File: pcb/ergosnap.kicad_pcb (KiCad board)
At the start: 2 copper layers, 133.6 x 132.2 mm, 41 parts, among them J0 Conn_01x05_Female, J1 5PIN, SW1 switch_diode, SW10 switch_diode, SW11 switch_diode, SW12 switch_diode, SW13 switch_diode, SW14 switch_diode, SW15 switch_diode, SW16 switch_diode, SW17 switch_diode, SW18 switch_diode, SW19 switch_diode, SW2 switch_diode, SW20 switch_diode, SW21 switch_diode, SW22 switch_diode, SW23 switch_diode, SW24 switch_diode, SW25 switch_diode, SW26 switch_diode, SW27 switch_diode, SW28 switch_diode, SW3 switch_diode, SW30 switch_diode, SW31 switch_diode, SW32 switch_diode, SW33 switch_diode, SW34 switch_diode, SW35 switch_diode, SW4 switch_diode, SW5 switch_diode, SW6 switch_diode, SW7 switch_diode, SW8 switch_diode, SW9 switch_diode, U3 ProMicro

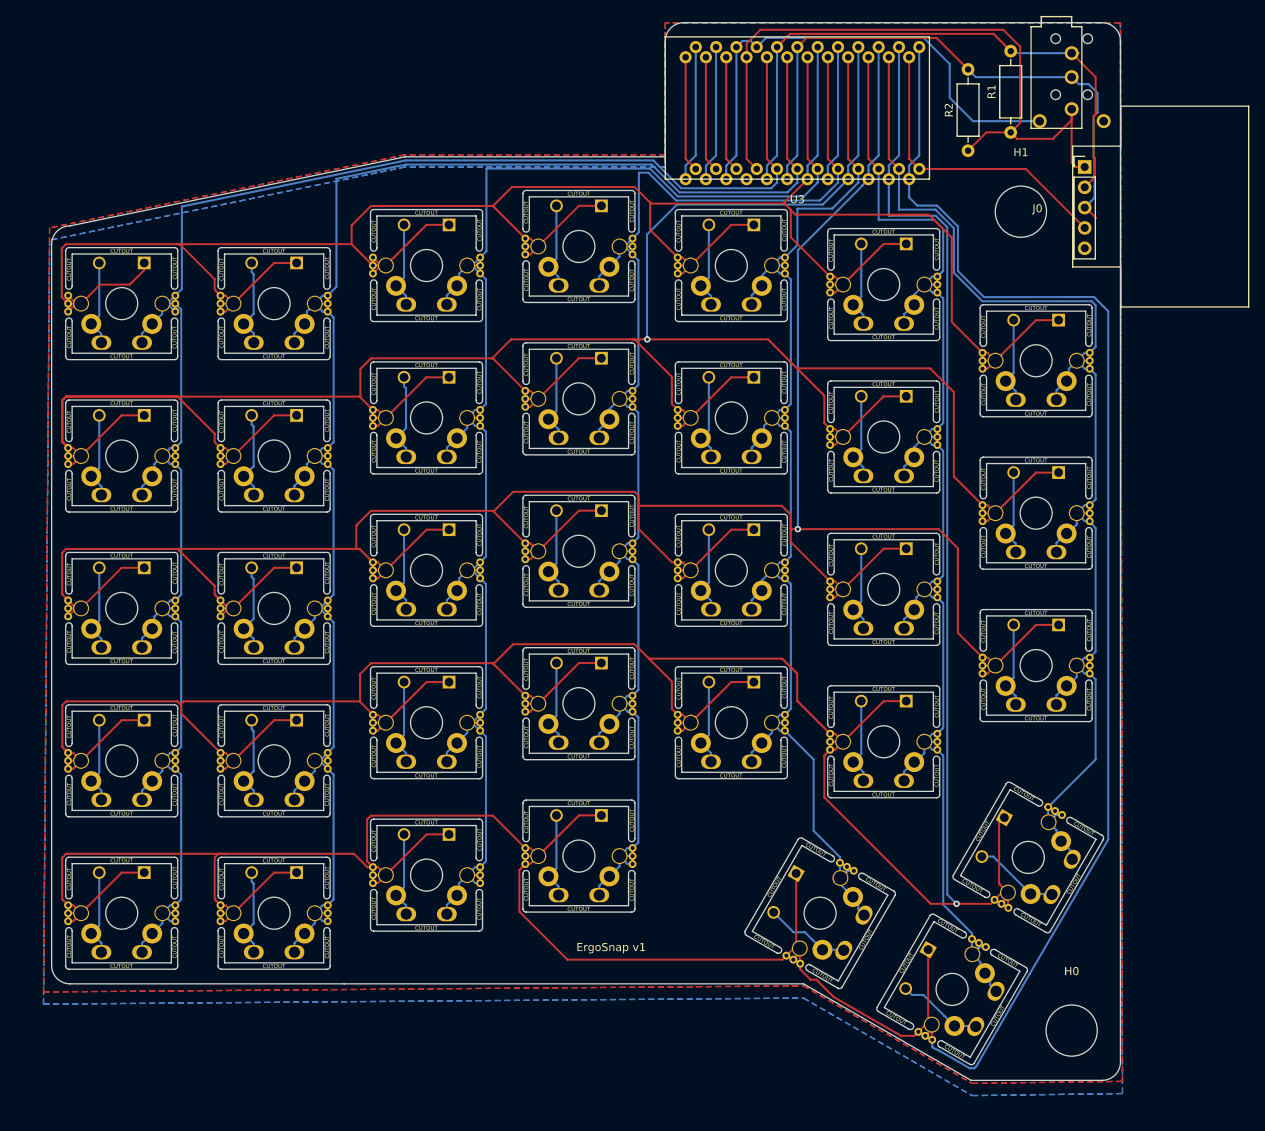
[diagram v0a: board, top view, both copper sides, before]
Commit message: Increase clearance between cutouts and board edge
Went for around 5mm, JLCPCB want a minimum of 3mm

Also rounded off the bottom right corner a bit more
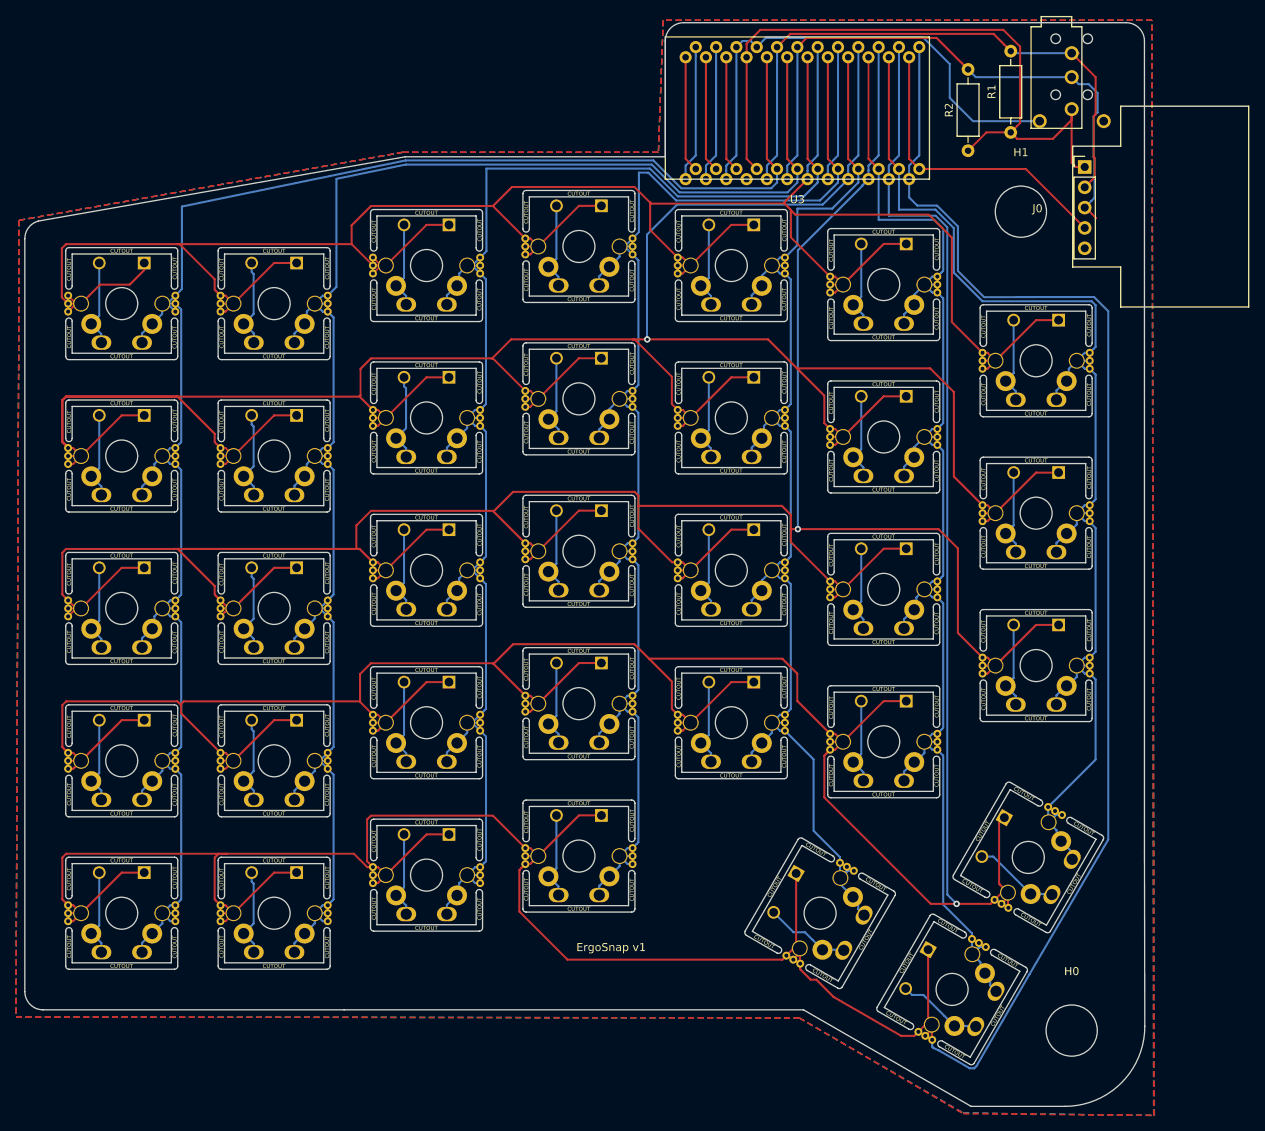
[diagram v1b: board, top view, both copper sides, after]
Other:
- board size 133.6 x 132.2 mm -> 140 x 135.5 mm
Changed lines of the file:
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@@
     (pad 1 np_thru_hole circle (at 0 0) (size 6.4 6.4) (drill 6.4) (layers *.Cu *.Mask))
   )
+  (gr_arc (start 204.878 148.317) (end 204.878 158.317) (angle -90) (layer Edge.Cuts) (width 0.15))
   (gr_text "ErgoSnap v1" (at 148.168 138.446) (layer B.SilkS)
     (effects (font (size 1 1) (thickness 0.15)) (justify mirror))
@@
     (effects (font (size 1 1) (thickness 0.15)))
   )
-  (gr_arc (start 209.55 152.781) (end 211.836 152.654) (angle 90) (layer Edge.Cuts) (width 0.15))
   (gr_line (start 154.94 39.624) (end 122.428 39.624) (layer Edge.Cuts) (width 0.15))
   (gr_line (start 154.94 25.146) (end 154.94 39.624) (layer Edge.Cuts) (width 0.15))
-  (gr_line (start 209.55 22.86) (end 157.226 22.86) (layer Edge.Cuts) (width 0.15))
-  (gr_line (start 211.836 58.674) (end 211.836 25.146) (layer Edge.Cuts) (width 0.15))
-  (gr_line (start 209.677 155.067) (end 193.167 155.067) (layer Edge.Cuts) (width 0.15))
-  (gr_line (start 211.836 126.619) (end 211.836 152.654) (layer Edge.Cuts) (width 0.15))
-  (gr_line (start 172.212 143.002) (end 193.167 155.067) (angle 90) (layer Edge.Cuts) (width 0.15))
-  (gr_line (start 211.836 122.174) (end 211.836 126.619) (angle 90) (layer Edge.Cuts) (width 0.15))
-  (gr_line (start 211.836 110.236) (end 211.836 122.174) (angle 90) (layer Edge.Cuts) (width 0.15))
-  (gr_line (start 211.836 58.674) (end 211.836 110.236) (angle 90) (layer Edge.Cuts) (width 0.15))
-  (gr_arc (start 209.55 25.146) (end 209.55 22.86) (angle 90) (layer Edge.Cuts) (width 0.15))
-  (gr_line (start 78.232 140.716) (end 78.232 50.546) (angle 90) (layer Edge.Cuts) (width 0.15))
-  (gr_line (start 80.518 143.002) (end 114.808 143.002) (angle 90) (layer Edge.Cuts) (width 0.15))
-  (gr_arc (start 80.518 140.716) (end 80.518 143.002) (angle 90) (layer Edge.Cuts) (width 0.15))
+  (gr_line (start 212.55 22.86) (end 157.226 22.86) (layer Edge.Cuts) (width 0.15))
+  (gr_line (start 214.836 58.674) (end 214.836 25.146) (layer Edge.Cuts) (width 0.15))
+  (gr_line (start 204.878 158.317) (end 193.167 158.317) (layer Edge.Cuts) (width 0.15))
+  (gr_line (start 214.836 126.619) (end 214.878 148.317) (layer Edge.Cuts) (width 0.15))
+  (gr_line (start 172.212 146.252) (end 193.167 158.317) (angle 90) (layer Edge.Cuts) (width 0.15))
+  (gr_line (start 214.836 122.174) (end 214.836 126.619) (angle 90) (layer Edge.Cuts) (width 0.15))
+  (gr_line (start 214.836 110.236) (end 214.836 122.174) (angle 90) (layer Edge.Cuts) (width 0.15))
+  (gr_line (start 214.836 58.674) (end 214.836 110.236) (angle 90) (layer Edge.Cuts) (width 0.15))
+  (gr_arc (start 212.55 25.146) (end 212.55 22.86) (angle 90) (layer Edge.Cuts) (width 0.15))
+  (gr_line (start 74.882 143.966) (end 74.882 49.864106) (angle 90) (layer Edge.Cuts) (width 0.15))
+  (gr_line (start 77.168 146.252) (end 114.808 146.252) (angle 90) (layer Edge.Cuts) (width 0.15))
+  (gr_arc (start 77.168 143.966) (end 77.168 146.252) (angle 90) (layer Edge.Cuts) (width 0.15))
   (gr_arc (start 157.226 25.146) (end 154.94 25.146) (angle 90) (layer Edge.Cuts) (width 0.15))
-  (gr_arc (start 80.518 50.546) (end 78.232 50.546) (angle 90) (layer Edge.Cuts) (width 0.15))
-  (gr_line (start 122.428 39.624) (end 80.518 48.26) (angle 90) (layer Edge.Cuts) (width 0.15))
-  (gr_line (start 114.808 143.002) (end 172.212 143.002) (angle 90) (layer Edge.Cuts) (width 0.15))
+  (gr_arc (start 77.168 49.864106) (end 74.882 49.864106) (angle 75) (layer Edge.Cuts) (width 0.15))
+  (gr_line (start 122.428 39.624) (end 76.57634 47.656) (angle 90) (layer Edge.Cuts) (width 0.15))
+  (gr_line (start 114.808 146.252) (end 172.212 146.252) (angle 90) (layer Edge.Cuts) (width 0.15))
   (segment (start 82.914999 56.975501) (end 81.915 57.9755) (width 0.254) (layer F.Cu) (net 1))
   (segment (start 84.296001 55.594499) (end 82.914999 56.975501) (width 0.254) (layer F.Cu) (net 1))
@@
     (polygon
       (pts
-        (xy 211.836 22.86) (xy 154.94 22.86) (xy 154.94 39.37) (xy 122.428 39.37) (xy 77.978 48.514)
-        (xy 77.216 144.018) (xy 172.212 143.256) (xy 193.294 155.448) (xy 212.09 155.194)
-      )
-    )
-  )
-  (zone (net 6) (net_name VCC) (layer B.Cu) (hatch edge 0.508)
-    (connect_pads (clearance 0.508))
-    (min_thickness 0.254)
-    (fill yes (arc_segments 32) (thermal_gap 0.508) (thermal_bridge_width 0.508))
-    (polygon
-      (pts
-        (xy 211.836 22.86) (xy 154.94 22.86) (xy 154.94 40.894) (xy 122.428 40.894) (xy 77.978 50.038)
-        (xy 77.216 145.542) (xy 172.212 144.78) (xy 193.294 156.972) (xy 212.09 156.718)
+        (xy 215.778 22.556) (xy 154.678 22.556) (xy 154.078 39.056) (xy 122.178 39.056) (xy 74.178 47.556)
+        (xy 73.778 147.156) (xy 171.678 147.256) (xy 192.178 159.156) (xy 216.078 159.456)
       )
     )
@@
     (polygon
       (pts
-        (xy 211.836 22.86) (xy 154.94 22.86) (xy 154.94 39.37) (xy 122.428 39.37) (xy 77.978 48.514)
-        (xy 77.216 144.018) (xy 172.212 143.256) (xy 193.294 155.448) (xy 212.09 155.194)
+        (xy 215.778 22.556) (xy 154.678 22.556) (xy 154.078 39.056) (xy 122.078 39.056) (xy 74.178 47.556)
+        (xy 73.778 147.156) (xy 171.678 147.256) (xy 192.178 159.256) (xy 215.978 159.456)
       )
     )
@@
     (polygon
       (pts
-        (xy 211.836 22.86) (xy 154.94 22.86) (xy 154.94 40.894) (xy 122.428 40.894) (xy 77.978 50.038)
-        (xy 77.216 145.542) (xy 172.212 144.78) (xy 193.294 156.972) (xy 212.09 156.718)
+        (xy 215.778 22.556) (xy 154.678 22.556) (xy 154.078 39.056) (xy 122.178 39.056) (xy 74.178 47.556)
+        (xy 73.778 147.141703) (xy 171.678 147.256) (xy 192.178 159.156) (xy 215.978 159.456)
       )
     )
+  )
+  (zone (net 6) (net_name VCC) (layer B.Cu) (hatch edge 0.508)
+    (connect_pads (clearance 0.508))
+    (min_thickness 0.254)
+    (fill yes (arc_segments 32) (thermal_gap 0.508) (thermal_bridge_width 0.508))
+    (polygon
+      (pts
+        (xy 215.778 22.556) (xy 154.678 22.556) (xy 154.078 39.056) (xy 122.178 39.056) (xy 74.178 47.556)
+        (xy 73.778 147.156) (xy 171.678 147.256) (xy 192.178 159.156) (xy 216.078 159.456)
+      )
+    )

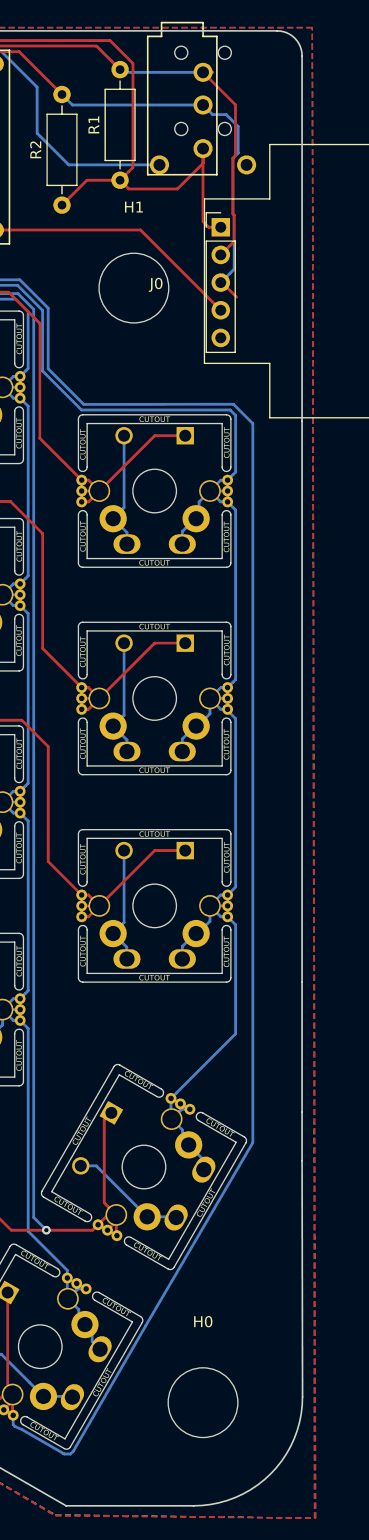
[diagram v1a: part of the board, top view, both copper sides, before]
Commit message: Tweak board outline a bit
Right hand edge now a single line and actually straight
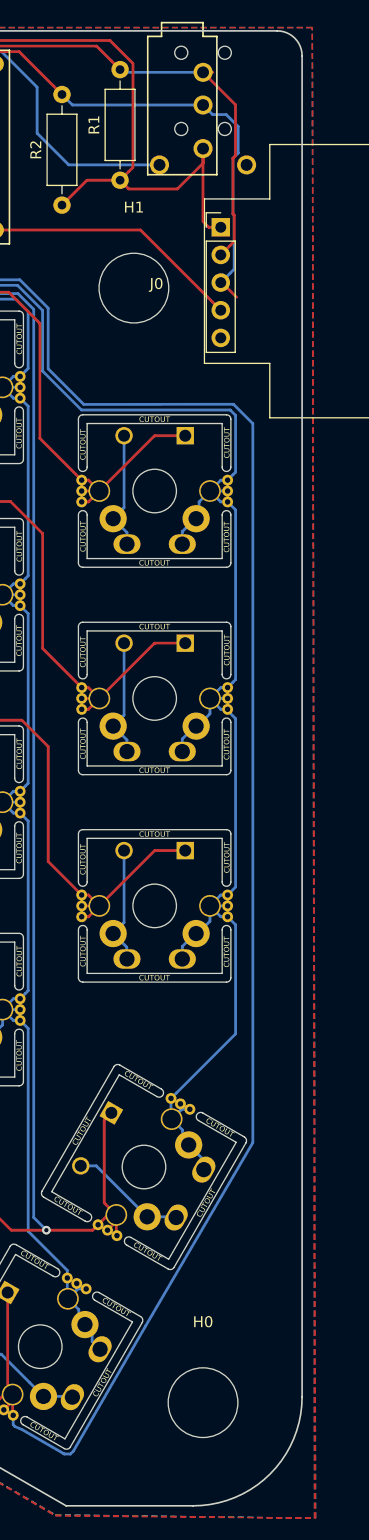
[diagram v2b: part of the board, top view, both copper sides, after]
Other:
- outline, holes or cut-outs redrawn
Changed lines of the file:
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@@
   (general
     (thickness 1.6)
-    (drawings 21)
+    (drawings 17)
     (tracks 1253)
     (zones 0)
@@
     (pad 1 np_thru_hole circle (at 0 0) (size 6.4 6.4) (drill 6.4) (layers *.Cu *.Mask))
   )
-  (gr_arc (start 204.878 148.317) (end 204.878 158.317) (angle -90) (layer Edge.Cuts) (width 0.15))
+  (gr_arc (start 204.836 148.317) (end 204.836 158.317) (angle -90) (layer Edge.Cuts) (width 0.15))
   (gr_text "ErgoSnap v1" (at 148.168 138.446) (layer B.SilkS)
     (effects (font (size 1 1) (thickness 0.15)) (justify mirror))
@@
   (gr_line (start 154.94 25.146) (end 154.94 39.624) (layer Edge.Cuts) (width 0.15))
   (gr_line (start 212.55 22.86) (end 157.226 22.86) (layer Edge.Cuts) (width 0.15))
-  (gr_line (start 214.836 58.674) (end 214.836 25.146) (layer Edge.Cuts) (width 0.15))
-  (gr_line (start 204.878 158.317) (end 193.167 158.317) (layer Edge.Cuts) (width 0.15))
-  (gr_line (start 214.836 126.619) (end 214.878 148.317) (layer Edge.Cuts) (width 0.15))
+  (gr_line (start 214.836 148.317) (end 214.836 25.146) (layer Edge.Cuts) (width 0.15))
+  (gr_line (start 204.836 158.317) (end 193.167 158.317) (layer Edge.Cuts) (width 0.15))
   (gr_line (start 172.212 146.252) (end 193.167 158.317) (angle 90) (layer Edge.Cuts) (width 0.15))
-  (gr_line (start 214.836 122.174) (end 214.836 126.619) (angle 90) (layer Edge.Cuts) (width 0.15))
-  (gr_line (start 214.836 110.236) (end 214.836 122.174) (angle 90) (layer Edge.Cuts) (width 0.15))
-  (gr_line (start 214.836 58.674) (end 214.836 110.236) (angle 90) (layer Edge.Cuts) (width 0.15))
   (gr_arc (start 212.55 25.146) (end 212.55 22.86) (angle 90) (layer Edge.Cuts) (width 0.15))
   (gr_line (start 74.882 143.966) (end 74.882 49.864106) (angle 90) (layer Edge.Cuts) (width 0.15))
